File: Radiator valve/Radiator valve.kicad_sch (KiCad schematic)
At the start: 22 parts, among them M1 Stepper_Motor, U2 ESP32-S3-MINI-1, U3 TLV1117-33, U4 BQ21040DBV, U5 MCP9501, U6 DRV8833PW

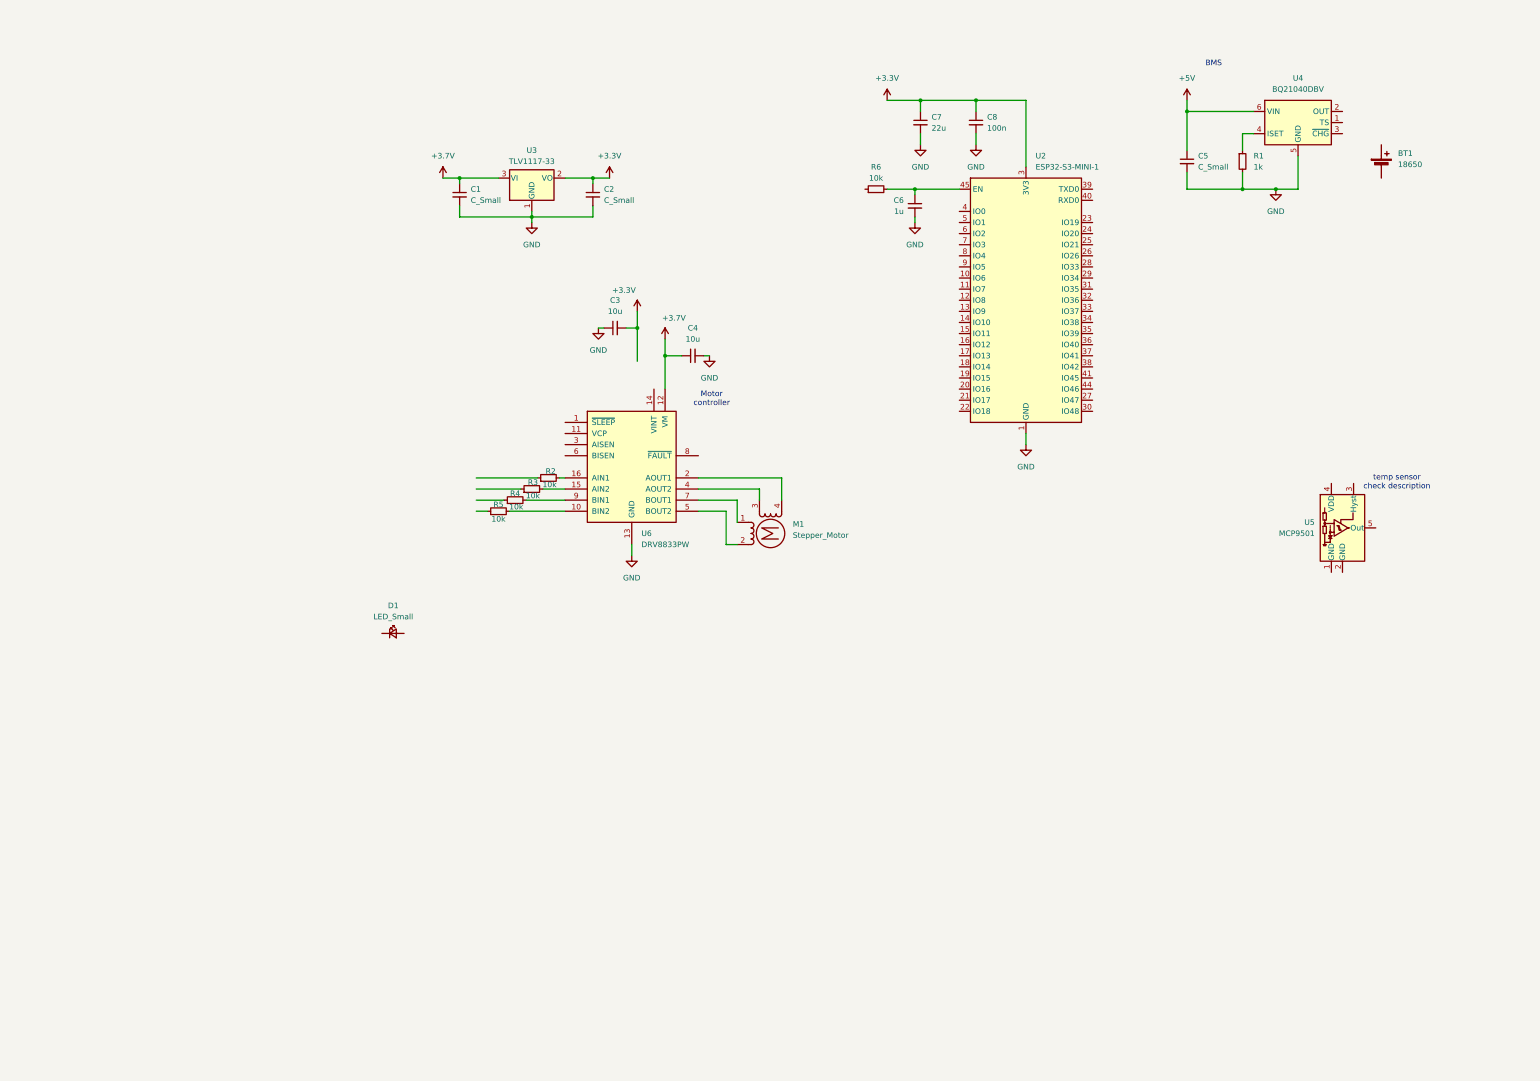
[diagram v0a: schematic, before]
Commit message: Dodany sensor
i coś jeszcze
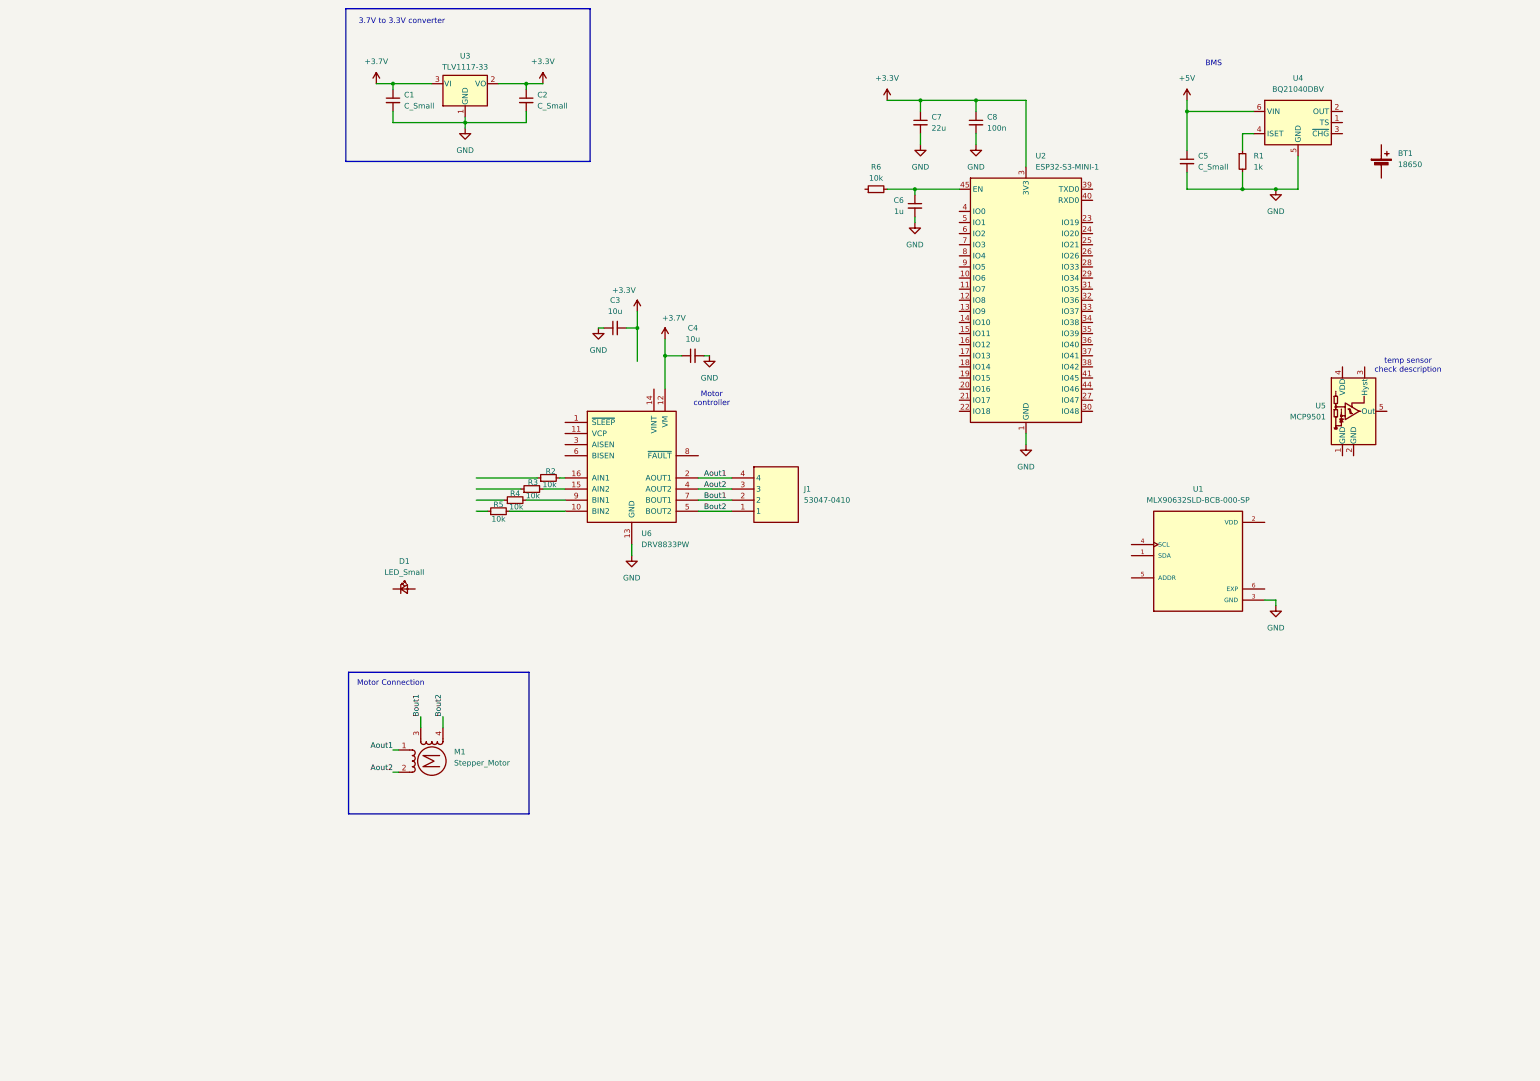
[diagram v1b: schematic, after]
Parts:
- added J1: 53047-0410, 530470410, symbol 53047-0410:53047-0410
- added U1: MLX90632SLD-BCB-000-SP, MLX90632SLD-BCB-000-SP:IC_MLX90632SLD-BCB-000-SP, symbol MLX90632SLD-BCB-000-SP:MLX90632SLD-BCB-000-SP
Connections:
- net GND: now also U1.3 (GND)
- net Aout1: now reaches M1.1
- net Aout1: now also U6.2 (AOUT1), J1.4; no longer U6.7 (BOUT1)
- net Aout2: now reaches M1.2 (-)
- net Aout2: now also U6.4 (AOUT2), J1.3; no longer U6.5 (BOUT2)
- net Bout1: now reaches M1.3
- net Bout1: now also U6.7 (BOUT1), J1.2; no longer U6.4 (AOUT2)
- net Bout2: now reaches M1.4
- net Bout2: now also U6.5 (BOUT2), J1.1; no longer U6.2 (AOUT1)
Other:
- note added: "3.7V to 3.3V converter"
- note added: "Motor Connection"
- moved on the sheet: C1, C2, D1, M1, U3, U5

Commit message: Schematic almost finished
Still minor fixes to do:
- check bms (undervoltage protection, ex. voltage divider)
- battery with pcm
- figure out how how to make this buck converter work
- battery and motor connector
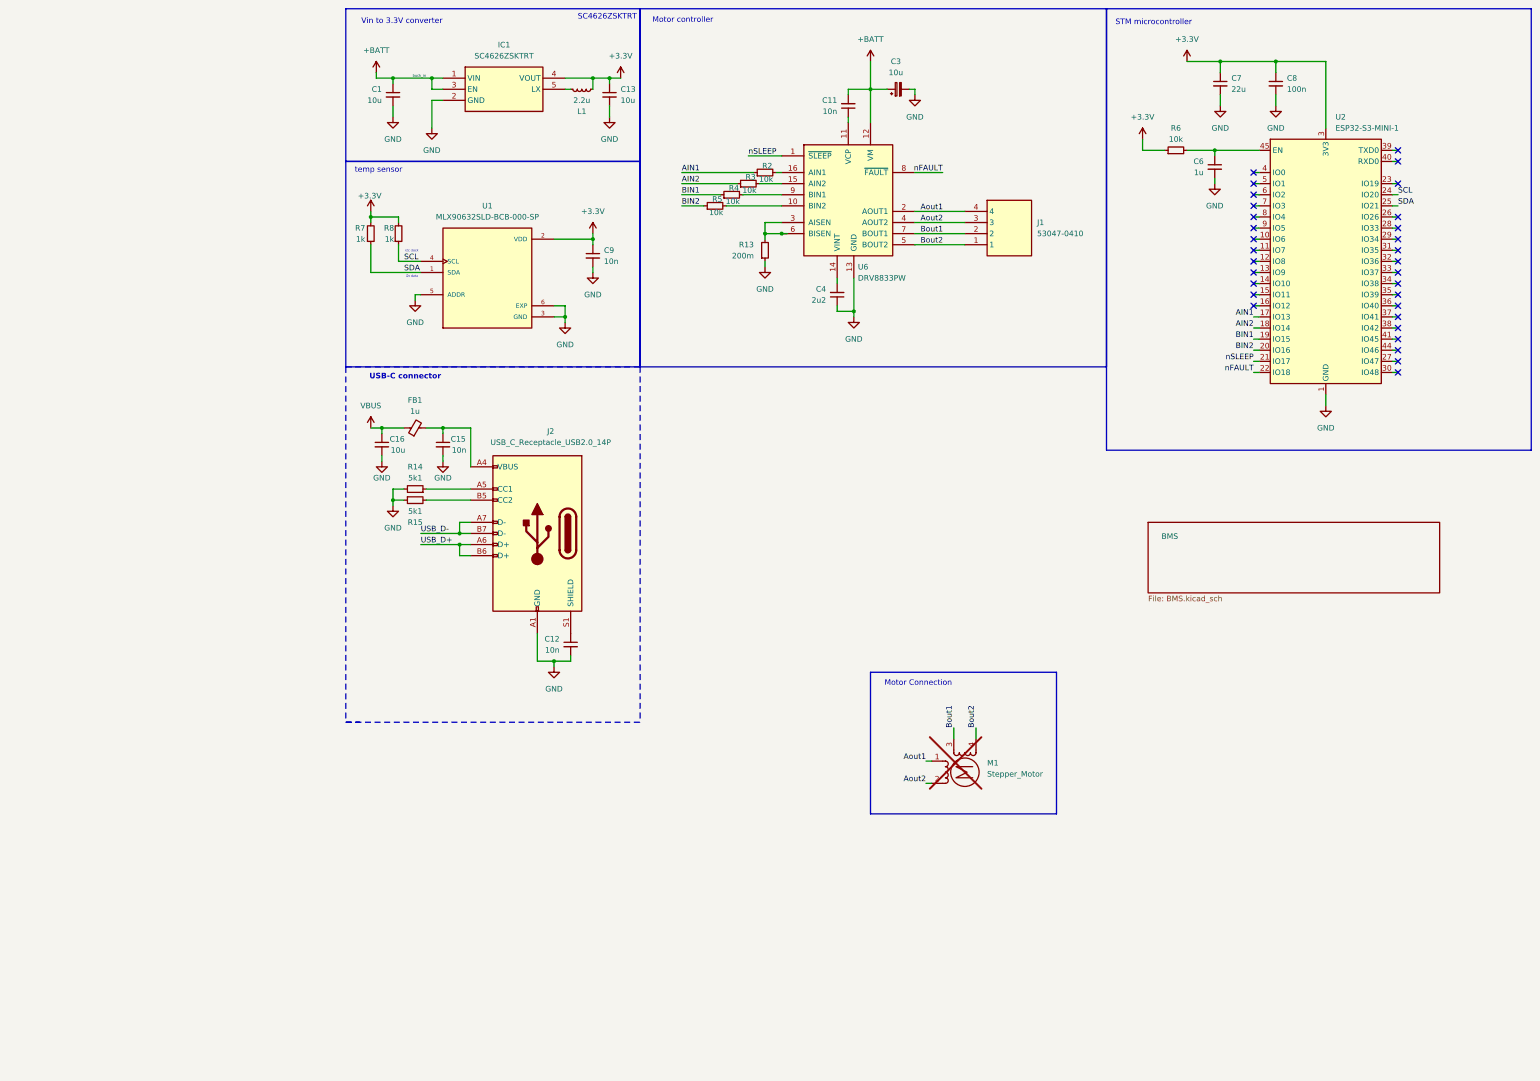
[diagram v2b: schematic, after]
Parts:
- removed BT1: 18650, symbol Device:Battery_Cell
- removed C2, C5: C_Small, symbol Device:C_Small
- removed C3: 10u, symbol Device:C_Small
- removed D1: LED_Small, symbol Device:LED_Small
- removed R1: 1k, symbol Device:R_Small
- removed U3: TLV1117-33, Package_TO_SOT_SMD:SOT-223, symbol Regulator_Linear:TLV1117-33
- removed U4: BQ21040DBV, Package_TO_SOT_SMD:SOT-23-6, symbol Battery_Management:BQ21040DBV
- removed U5: MCP9501, Package_TO_SOT_SMD:SOT-23-5, symbol Sensor_Temperature:MCP9501
- added C11, C12, C15, C9: 10n, Capacitor_SMD:C_0603_1608Metric, symbol Device:C_Small
- added C13: 10u, Capacitor_SMD:C_0805_2012Metric, symbol Device:C_Small
- added C16: 10u, Capacitor_SMD:C_0603_1608Metric, symbol Device:C_Small
- added C3: 10u, symbol Device:C_Polarized_Small
- added FB1: 1u, Inductor_SMD:L_0603_1608Metric, symbol Device:FerriteBead_Small
- added IC1: SC4626ZSKTRT, SOT95P280X145-5N, symbol SC4626ZSKTRT:SC4626ZSKTRT
- added J2: USB_C_Receptacle_USB2.0_14P, Connector_USB:USB_C_Receptacle_GCT_USB4125-xx-x-0190_6P_TopMnt_Horizontal, symbol Connector:USB_C_Receptacle_USB2.0_14P
- added L1: 2.2u, Inductor_SMD:L_0805_2012Metric, symbol Device:L_Small
- added R13: 200m, Resistor_SMD:R_0603_1608Metric, symbol Device:R_Small
- added R14, R15: 5k1, Resistor_SMD:R_0603_1608Metric, symbol Device:R_Small
- added R7, R8: 1k, Resistor_SMD:R_0603_1608Metric, symbol Device:R_Small
- C1: value C_Small -> 10u; footprint (none) -> Capacitor_SMD:C_0603_1608Metric; m (none) -> https://www.mouser.pl/ProductDetail/KYOCERA-AVX/KGM21AR71A1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
- C4: value 10u -> 2u2; footprint (none) -> Capacitor_SMD:C_0603_1608Metric
- C6: footprint (none) -> Capacitor_SMD:C_0603_1608Metric
- M1: now not fitted
- R2, R3, R4, R5, R6: footprint (none) -> Resistor_SMD:R_0603_1608Metric
- U1: footprint MLX90632SLD-BCB-000-SP:IC_MLX90632SLD-BCB-000-SP -> MLX90632:IC_MLX90632SLD-BCB-000-SP
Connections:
- net +3.3V: now also R6.1, U1.2 (VDD), C13.1, C9.1, IC1.4 (VOUT), L1.2, R7.2, R8.2
- net GND: now also C4.1, U1.5 (ADDR), U1.6 (EXP), C12.2, C13.2, C15.2, C16.2, C3.2, C9.2, IC1.2 (GND), J2.A1 (GND), J2.A12 (GND), J2.B1 (GND), J2.B12 (GND), R13.1, R14.2, R15.1; no longer C4.2
- net AIN2: now reaches R3.1
- net AIN2: now also U2.18 (IO14)
- net AIN1: now reaches R2.1
- net AIN1: now also U2.17 (IO13)
- net BIN2: now reaches R5.1
- net BIN2: now also U2.20 (IO16)
- net SDA: now reaches U1.1 (SDA)
- net SDA: now also U2.25 (IO21), R7.1
- net SCL: now reaches U1.4 (SCL)
- net SCL: now also U2.24 (IO20), R8.1
- net BIN1: now reaches U2.19 (IO15)
- net BIN1: now also R4.1
- net nSLEEP: now reaches U2.21 (IO17)
- net nSLEEP: now also U6.1 (~{SLEEP})
- net nFAULT: now reaches U2.22 (IO18)
- net nFAULT: now also U6.8 (~{FAULT})
- net at U6.11 (VCP): now also C11.1
- net at U6.14 (VINT): now also C4.2
- net at U6.3 (AISEN): now also U6.6 (BISEN), R13.2
- net +3.7V renamed +BATT
- net +BATT: now also C11.2, C3.1, IC1.1 (VIN), IC1.3 (EN); no longer C4.1
- new net: IC1.5 (LX), L1.1
- new net: C12.1, J2.S1 (SHIELD)
- new net: J2.B5 (CC2), R15.2
- new net: J2.A5 (CC1), R14.1
- new net: C15.1, FB1.2, J2.A4 (VBUS), J2.A9 (VBUS), J2.B4 (VBUS), J2.B9 (VBUS)
- new net USB_D+: J2.A6 (D+), J2.B6 (D+)
- new net USB_D-: J2.A7 (D-), J2.B7 (D-)
- new net VBUS: C16.1, FB1.1
- no-connect marks 0 -> 31
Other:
- added sheet BMS (BMS.kicad_sch)
- note added: "SC4626ZSKTRT"
- note added: "STM microcontroller"
- note added: "USB-C connector"
- note added: "Vin to 3.3V converter"
- note added: "i2c clock"
- note added: "i2c data"
- note added: "temp sensor"
- note removed: "3.7V to 3.3V converter"
- note removed: "BMS"
- note removed: "temp sensor check description"
- moved on the sheet: C1, C6, C7, C8, J1, R2, R6, U1, U2, U6

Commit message: Finished schematic
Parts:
- removed C3: 10u, symbol Device:C_Polarized_Small
- removed FB1: 1u, Inductor_SMD:L_0603_1608Metric, symbol Device:FerriteBead_Small
- added BT1: 18650, symbol Device:Battery_Cell
- added C10: 100n, Capacitor_SMD:C_0402_1005Metric, symbol Device:C_Small
- added C14, C18: 4.7u, Capacitor_SMD:C_0603_1608Metric, symbol Device:C_Small
- added C17, C19: 10u, Capacitor_SMD:C_0402_1005Metric, symbol Device:C_Small
- added C2: 10u, Capacitor_SMD:C_0603_1608Metric, symbol Device:C_Small
- added C3: 10n, Capacitor_SMD:C_0603_1608Metric, symbol Device:C_Small
- added C5: 1u, Capacitor_SMD:C_0603_1608Metric, symbol Device:C_Small
- added D1, D2: LED_Small, LED_SMD:LED_0402_1005Metric, symbol Device:LED_Small
- added D3, D4: PESD5V0S1UL,315, Diode_SMD:D_SOD-523, symbol Diode:ESD5Zxx
- added J3: Conn_01x02, symbol Connector_Generic:Conn_01x02
- added L2: 1.5u, Inductor_SMD:L_Coilcraft_LPS3010, symbol Device:L
- added R1: 10k, Resistor_SMD:R_0402_1005Metric, symbol Device:R_Small
- added R10: 1.13k, Resistor_SMD:R_0402_1005Metric, symbol Device:R_Small
- added R11, R12: 1k, Resistor_SMD:R_0402_1005Metric, symbol Device:R_Small
- added R9: 1.18k, Resistor_SMD:R_0402_1005Metric, symbol Device:R_Small
- added TH1: 10k, symbol Device:Thermistor_NTC
- added U3: TPS63031DSK, Package_SON:WSON-10-1EP_2.5x2.5mm_P0.5mm_EP1.2x2mm, symbol Regulator_Switching:TPS63031DSK
- added U4: BQ24075RGT, Package_DFN_QFN:VQFN-16-1EP_3x3mm_P0.5mm_EP1.6x1.6mm, symbol Battery_Management:BQ24075RGT
- C1, C13, IC1, L1: now not fitted; now left out of the parts list
- C11: m (none) -> https://www.mouser.pl/ProductDetail/Murata-Electronics/GCJ1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; model (none) -> GCJ188R71C103KA01D
- C4: m (none) -> https://www.mouser.pl/ProductDetail/KYOCERA-AVX/06036D225KA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; model (none) -> 06036D225KAT2A
- C7, C8: footprint Capacitor_SMD:C_0603_1608Metric -> Capacitor_SMD:C_0402_1005Metric
- J2: footprint Connector_USB:USB_C_Receptacle_GCT_USB4125-xx-x-0190_6P_TopMnt_Horizontal -> Connector_USB:USB_C_Receptacle_GCT_USB4110
- M1: Field5 http://www.infineon.com/dgdl/Application-Note-TLE8110EE_dri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 -> (none); m (none) -> https://www.omc-stepperonline.com/nema-8-bipolar-1-8deg-3nc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
- R13: footprint Resistor_SMD:R_0603_1608Metric -> Resistor_SMD:R_0402_1005Metric; m (none) -> https://www.mouser.pl/ProductDetail/Panasonic/ERJ-3BSJR20V?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; model (none) -> ERJ-3BSJR20V
- R14, R2, R3, R4, R7, R8: footprint Resistor_SMD:R_0603_1608Metric -> Resistor_SMD:R_0402_1005Metric
- R15: value 5k1 -> 10k; footprint Resistor_SMD:R_0603_1608Metric -> Resistor_SMD:R_0402_1005Metric
- R5: value 10k -> 5k1; footprint Resistor_SMD:R_0603_1608Metric -> Resistor_SMD:R_0402_1005Metric
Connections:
- net +3.3V: now also R15.1, C17.2, C19.2, U3.1 (VOUT), U3.10 (FB)
- net +BATT: now also C10.2, C14.1, C2.2, C3.2, R11.1, R12.1, U3.5 (VIN), U3.6 (EN), U3.8 (VINA), U4.10 (OUT), U4.11 (OUT), U4.5 (EN2)
- net AIN2: now also R1.1; no longer R3.1
- net BIN1: now also R3.1; no longer R4.1
- net BIN2: now also R4.1; no longer R5.1
- net GND: now also R5.2, BT1.2 (-), C10.1, C14.2, C17.1, C18.2, C19.1, C2.1, C3.1, C5.1, D3.2 (A), D4.2 (A), R10.1, R9.2, TH1.1, U3.11 (PGND), U3.3 (PGND), U3.7 (PS/SYNC), U3.9 (GND), U4.14 (TMR), U4.17 (VSS), U4.4 (~{CE}), U4.6 (EN1), U4.8 (VSS); no longer R15.1
- net USB_D+: now also D4.1 (K)
- net USB_D-: now also D3.1 (K)
- net VBUS: now also C15.1, J2.A4 (VBUS), J2.A9 (VBUS), J2.B4 (VBUS), J2.B9 (VBUS), C5.2, U4.13 (IN)
- net nSLEEP: now also R15.2
- net at U6.10 (BIN2): now also R4.2; no longer R5.2
- net at U6.9 (BIN1): now also R3.2; no longer R4.2
- net at J2.B5 (CC2): now also R5.1; no longer R15.2
- net at U6.15 (AIN2): now also R1.2; no longer R3.2
- new net: D2.2 (A), R12.2
- new net: R9.1, U4.12 (ILIM)
- new net: R10.2, U4.16 (ISET)
- new net: D1.1 (K), U4.7 (~{PGOOD})
- new net: D2.1 (K), U4.9 (~{CHG})
- new net: D1.2 (A), R11.2
- new net: L2.1, U3.2 (L2)
- new net: L2.2, U3.4 (L1)
- new net bat+: BT1.1 (+), C18.1, J3.2 (Pin_2), U4.2 (BAT), U4.3 (BAT)
- new net bat-: J3.1 (Pin_1), TH1.2, U4.1 (TS)
- no-connect marks 31 -> 32
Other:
- removed sheet BMS
- note added: "BMS"
- note added: "Battery pack"
- note added: "Buck-boost converter"
- note added: "m: link do mousera model: nazwa komponentu w mouserze"
- note added: "stm controlling on off state"
- note removed: "SC4626ZSKTRT"
- note removed: "Vin to 3.3V converter"
- moved on the sheet: C11, C12, C15, C16, C4, C9, J1, J2, M1, R13, R14, R2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

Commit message: Layout started
Pushed for BOM
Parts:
- removed C1: 10u, Capacitor_SMD:C_0603_1608Metric, symbol Device:C_Small
- removed C13: 10u, Capacitor_SMD:C_0805_2012Metric, symbol Device:C_Small
- removed IC1: SC4626ZSKTRT, SOT95P280X145-5N, symbol SC4626ZSKTRT:SC4626ZSKTRT
- removed J3: Conn_01x02, symbol Connector_Generic:Conn_01x02
- removed L1: 2.2u, Inductor_SMD:L_0805_2012Metric, symbol Device:L_Small
- added J4: Conn_01x03, Connector_Molex:Molex_PicoBlade_53261-0371_1x03-1MP_P1.25mm_Horizontal, symbol Connector_Generic:Conn_01x03
- C6: footprint Capacitor_SMD:C_0603_1608Metric -> Capacitor_SMD:C_0402_1005Metric
- D1, D2: value LED_Small -> LTST-C281KRKT
- J1: footprint 530470410 -> Connector_Molex:Molex_PicoBlade_53047-0410_1x04_P1.25mm_Vertical
- J2: value USB_C_Receptacle_USB2.0_14P -> USB4105-GF-A-120; footprint Connector_USB:USB_C_Receptacle_GCT_USB4110 -> Connector_USB:USB_C_Receptacle_GCT_USB4105-xx-A_16P_TopMnt_Horizontal; m (none) -> https://www.mouser.pl/ProductDetail/GCT/USB4105-GF-A-120?qs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
- R6: footprint Resistor_SMD:R_0603_1608Metric -> Resistor_SMD:R_0402_1005Metric
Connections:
- net AIN1: now also U2.20 (IO16); no longer U2.17 (IO13)
- net AIN2: now also U2.19 (IO15); no longer U2.18 (IO14)
- net BIN1: now also U2.18 (IO14); no longer U2.19 (IO15)
- net BIN2: now also U2.17 (IO13); no longer U2.20 (IO16)
- net Bout1: now also J1.1; no longer J1.2
- net Bout2: now also J1.2; no longer J1.1
- net GND: now also J4.2 (Pin_2)
- net SCL: now also U2.37 (IO41); no longer U2.24 (IO20)
- net SDA: now also U2.38 (IO42); no longer U2.25 (IO21)
- net USB_D+: now also U2.24 (IO20)
- net USB_D-: now also U2.23 (IO19)
- net bat+: now also J4.3 (Pin_3)
- net bat- renamed ts
- net ts: now also J4.1 (Pin_1)
- no-connect marks 32 -> 26
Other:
- moved on the sheet: J1
